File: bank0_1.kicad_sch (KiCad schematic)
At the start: 1 part, among them IC1 ECP5-BGA256

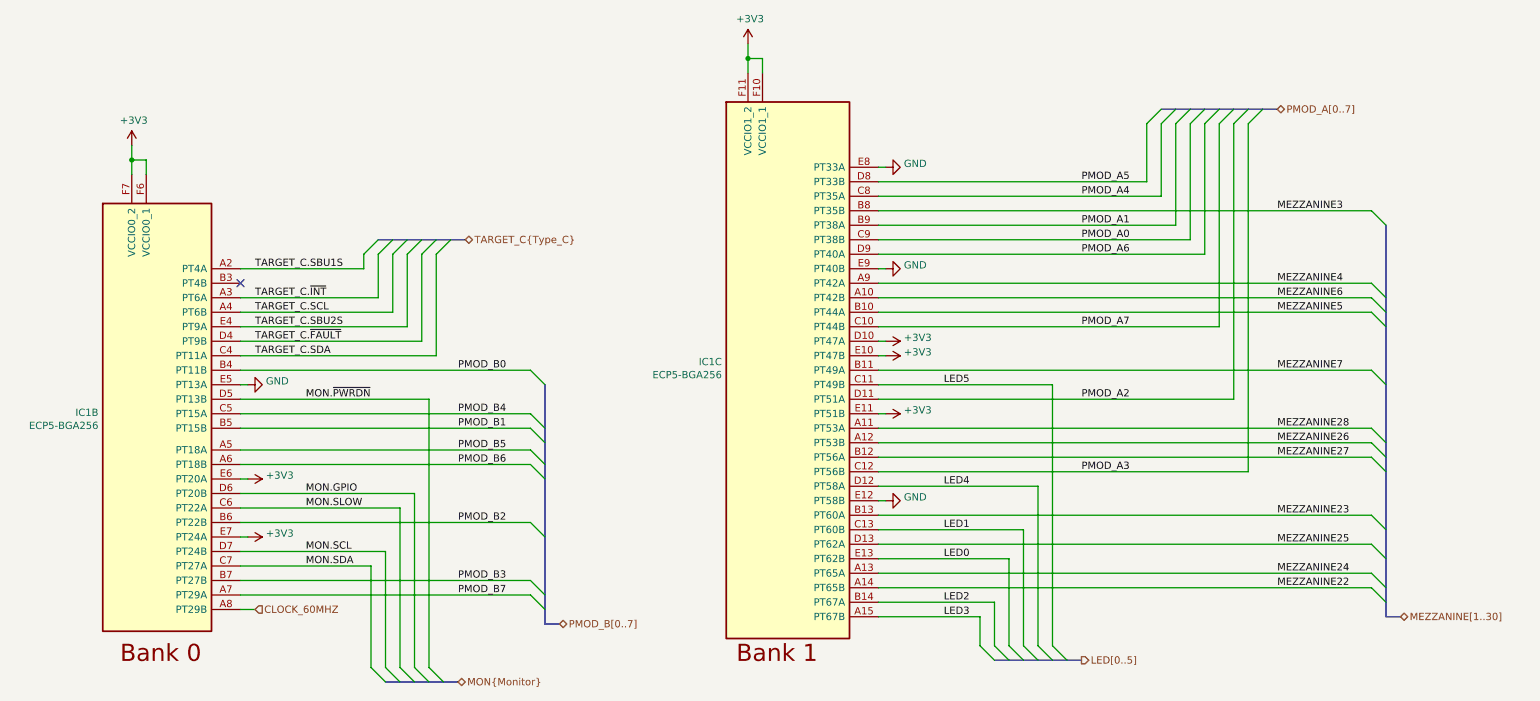
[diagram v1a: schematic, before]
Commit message: Clean up schematic
- Renumber Pmod signal names to match silkscreen labels
- Clean up FPGA symbol
- Clean up PHY symbol
- Add title block to newer sheets
- Fix horizontal line in LED sheet
- Improve various label positions
- Update data sheet fields
- Renumber pages
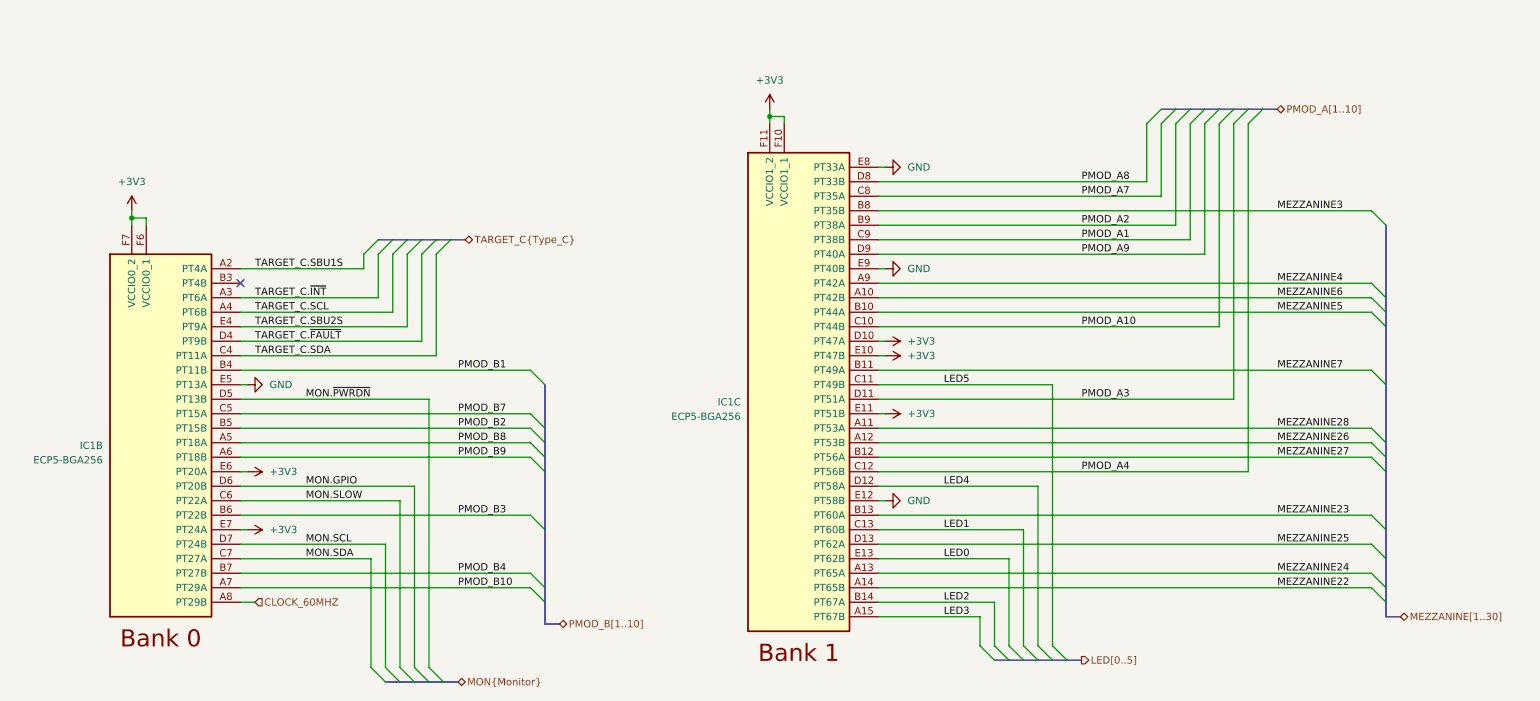
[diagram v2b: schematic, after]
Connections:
- net PMOD_A0 is gone; now on net PMOD_A1: IC1.C9 (PT38B)
- net PMOD_B0 is gone; now on net PMOD_B1: IC1.B4 (PT11B)
- net PMOD_A1: no longer IC1.B9 (PT38A)
- net PMOD_A2: now also IC1.B9 (PT38A); no longer IC1.D11 (PT51A)
- net PMOD_A3: now also IC1.D11 (PT51A); no longer IC1.C12 (PT56B)
- net PMOD_A4: now also IC1.C12 (PT56B); no longer IC1.C8 (PT35A)
- net PMOD_A7: now also IC1.C8 (PT35A); no longer IC1.C10 (PT44B)
- net PMOD_B1: no longer IC1.B5 (PT15B)
- net PMOD_B2: now also IC1.B5 (PT15B); no longer IC1.B6 (PT22B)
- net PMOD_B3: now also IC1.B6 (PT22B); no longer IC1.B7 (PT27B)
- net PMOD_B4: now also IC1.B7 (PT27B); no longer IC1.C5 (PT15A)
- net PMOD_B7: now also IC1.C5 (PT15A); no longer IC1.A7 (PT29A)
- net PMOD_A5 renamed PMOD_A8
- net PMOD_A6 renamed PMOD_A9
- net PMOD_B5 renamed PMOD_B8
- net PMOD_B6 renamed PMOD_B9
- new net PMOD_A10: IC1.C10 (PT44B)
- new net PMOD_B10: IC1.A7 (PT29A)
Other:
- moved on the sheet: IC1B, IC1C

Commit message: Update copyright notices
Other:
- company: Copyright 2019-2023 Great Scott Gadgets -> ${COPYRIGHT}
- title: Cynthion -> ${TITLE}
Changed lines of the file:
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@@
   (paper "A4")
   (title_block
-    (title "Cynthion")
+    (title "${TITLE}")
     (date "${DATE}")
     (rev "${VERSION}")
-    (company "Copyright 2019-2023 Great Scott Gadgets")
-    (comment 1 "Licensed under the CERN-OHL-P v2")
+    (company "${COPYRIGHT}")
+    (comment 1 "${LICENSE}")
   )
   (junction (at 35.56 59.69) (diameter 0) (color 0 0 0 0)
